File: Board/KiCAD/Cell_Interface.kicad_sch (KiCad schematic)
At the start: 26 parts, among them Q23 2N7002, Q24 2N7002, Q25 2N7002, Q26 2N7002, Q5 BSS83P, Q6 BSS83P, Q7 BSS83P, Q8 BSS83P, U6 INA219AxDCN, U7 INA219AxDCN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

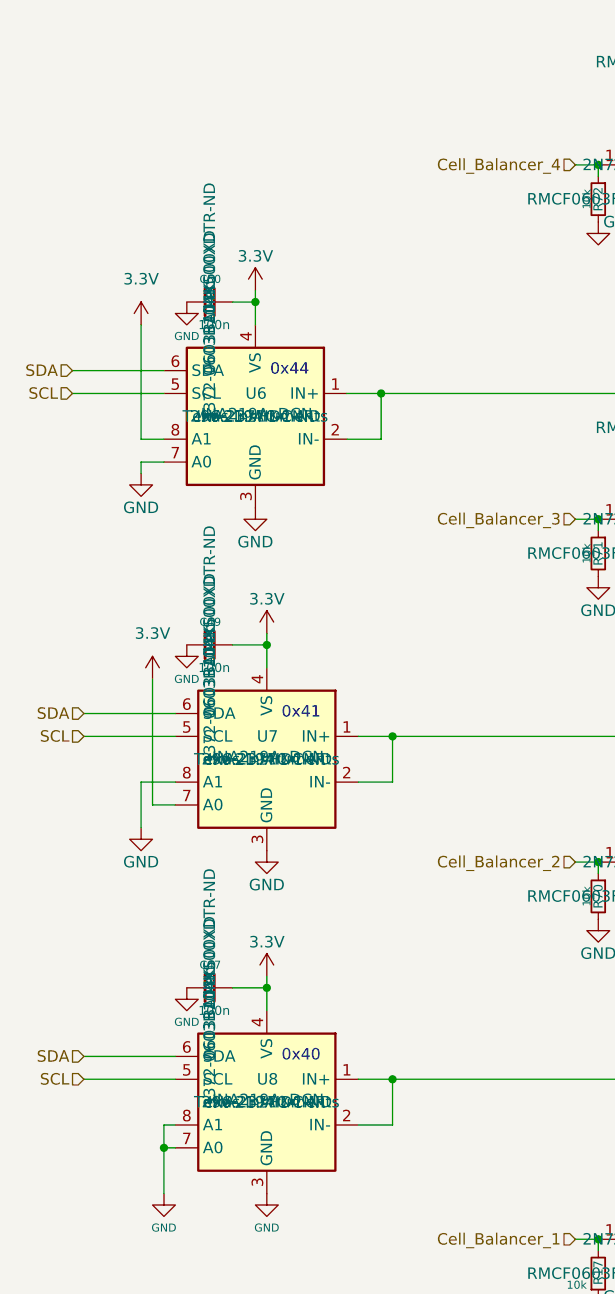
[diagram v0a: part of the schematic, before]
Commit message: Updated BOM as Per Ed's Request
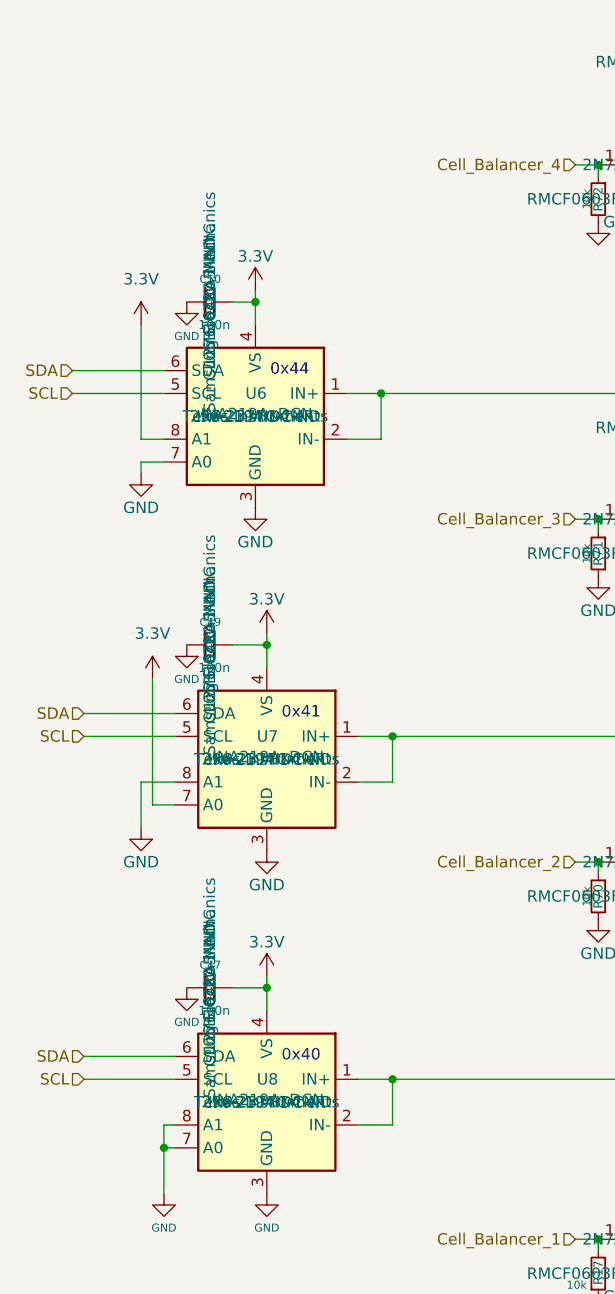
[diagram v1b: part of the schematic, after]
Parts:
- C47, C49, C50: MFR Aillen -> Samsung Electro-Mechanics; MPN 3372-0603B104K500XDTR-ND -> 1276-6720-1-ND; Package 0603B104K500XD -> CL05B104KA5NNNC
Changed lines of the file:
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@@
 			)
 		)
-		(property "Datasheet" "https://mm.digikey.com/Volume0/opasdata/d220001/medias/docus/6490/3372_0603B104K500XD.pdf"
+		(property "Datasheet" "https://mm.digikey.com/Volume0/opasdata/d220001/medias/docus/729/CL05B104KA5NNNC_Spec.pdf"
 			(at 63.5 137.16 0)
 			(effects
@@
 			)
 		)
-		(property "MFR" "Aillen"
+		(property "MFR" "Samsung Electro-Mechanics"
 			(at 63.5 137.16 0)
 			(effects
@@
 			)
 		)
-		(property "MPN" "3372-0603B104K500XDTR-ND"
+		(property "MPN" "1276-6720-1-ND"
 			(at 63.5 137.16 0)
 			(effects
@@
 			)
 		)
-		(property "Package" "0603B104K500XD"
+		(property "Package" "CL05B104KA5NNNC"
 			(at 63.5 137.16 0)
 			(effects
@@
 			)
 		)
-		(property "Datasheet" "https://mm.digikey.com/Volume0/opasdata/d220001/medias/docus/6490/3372_0603B104K500XD.pdf"
+		(property "Datasheet" "https://mm.digikey.com/Volume0/opasdata/d220001/medias/docus/729/CL05B104KA5NNNC_Spec.pdf"
 			(at 63.5 99.06 0)
 			(effects
@@
 			)
 		)
-		(property "MFR" "Aillen"
+		(property "MFR" "Samsung Electro-Mechanics"
 			(at 63.5 99.06 0)
 			(effects
@@
 			)
 		)
-		(property "MPN" "3372-0603B104K500XDTR-ND"
+		(property "MPN" "1276-6720-1-ND"
 			(at 63.5 99.06 0)
 			(effects
@@
 			)
 		)
-		(property "Package" "0603B104K500XD"
+		(property "Package" "CL05B104KA5NNNC"
 			(at 63.5 99.06 0)
 			(effects
@@
 			)
 		)
-		(property "Datasheet" "https://mm.digikey.com/Volume0/opasdata/d220001/medias/docus/6490/3372_0603B104K500XD.pdf"
+		(property "Datasheet" "https://mm.digikey.com/Volume0/opasdata/d220001/medias/docus/729/CL05B104KA5NNNC_Spec.pdf"
 			(at 63.5 60.96 0)
 			(effects
@@
 			)
 		)
-		(property "MFR" "Aillen"
+		(property "MFR" "Samsung Electro-Mechanics"
 			(at 63.5 60.96 0)
 			(effects
@@
 			)
 		)
-		(property "MPN" "3372-0603B104K500XDTR-ND"
+		(property "MPN" "1276-6720-1-ND"
 			(at 63.5 60.96 0)
 			(effects
@@
 			)
 		)
-		(property "Package" "0603B104K500XD"
+		(property "Package" "CL05B104KA5NNNC"
 			(at 63.5 60.96 0)
 			(effects

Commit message: non corrupt ver.
safsfs
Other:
- note added: "Edited"
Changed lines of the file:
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@@
+		)
+	)
+	(text "Edited"
+		(exclude_from_sim no)
+		(at 170.688 68.326 0)
+		(effects
+			(font
+				(size 1.27 1.27)
+			)
 		)
 	)

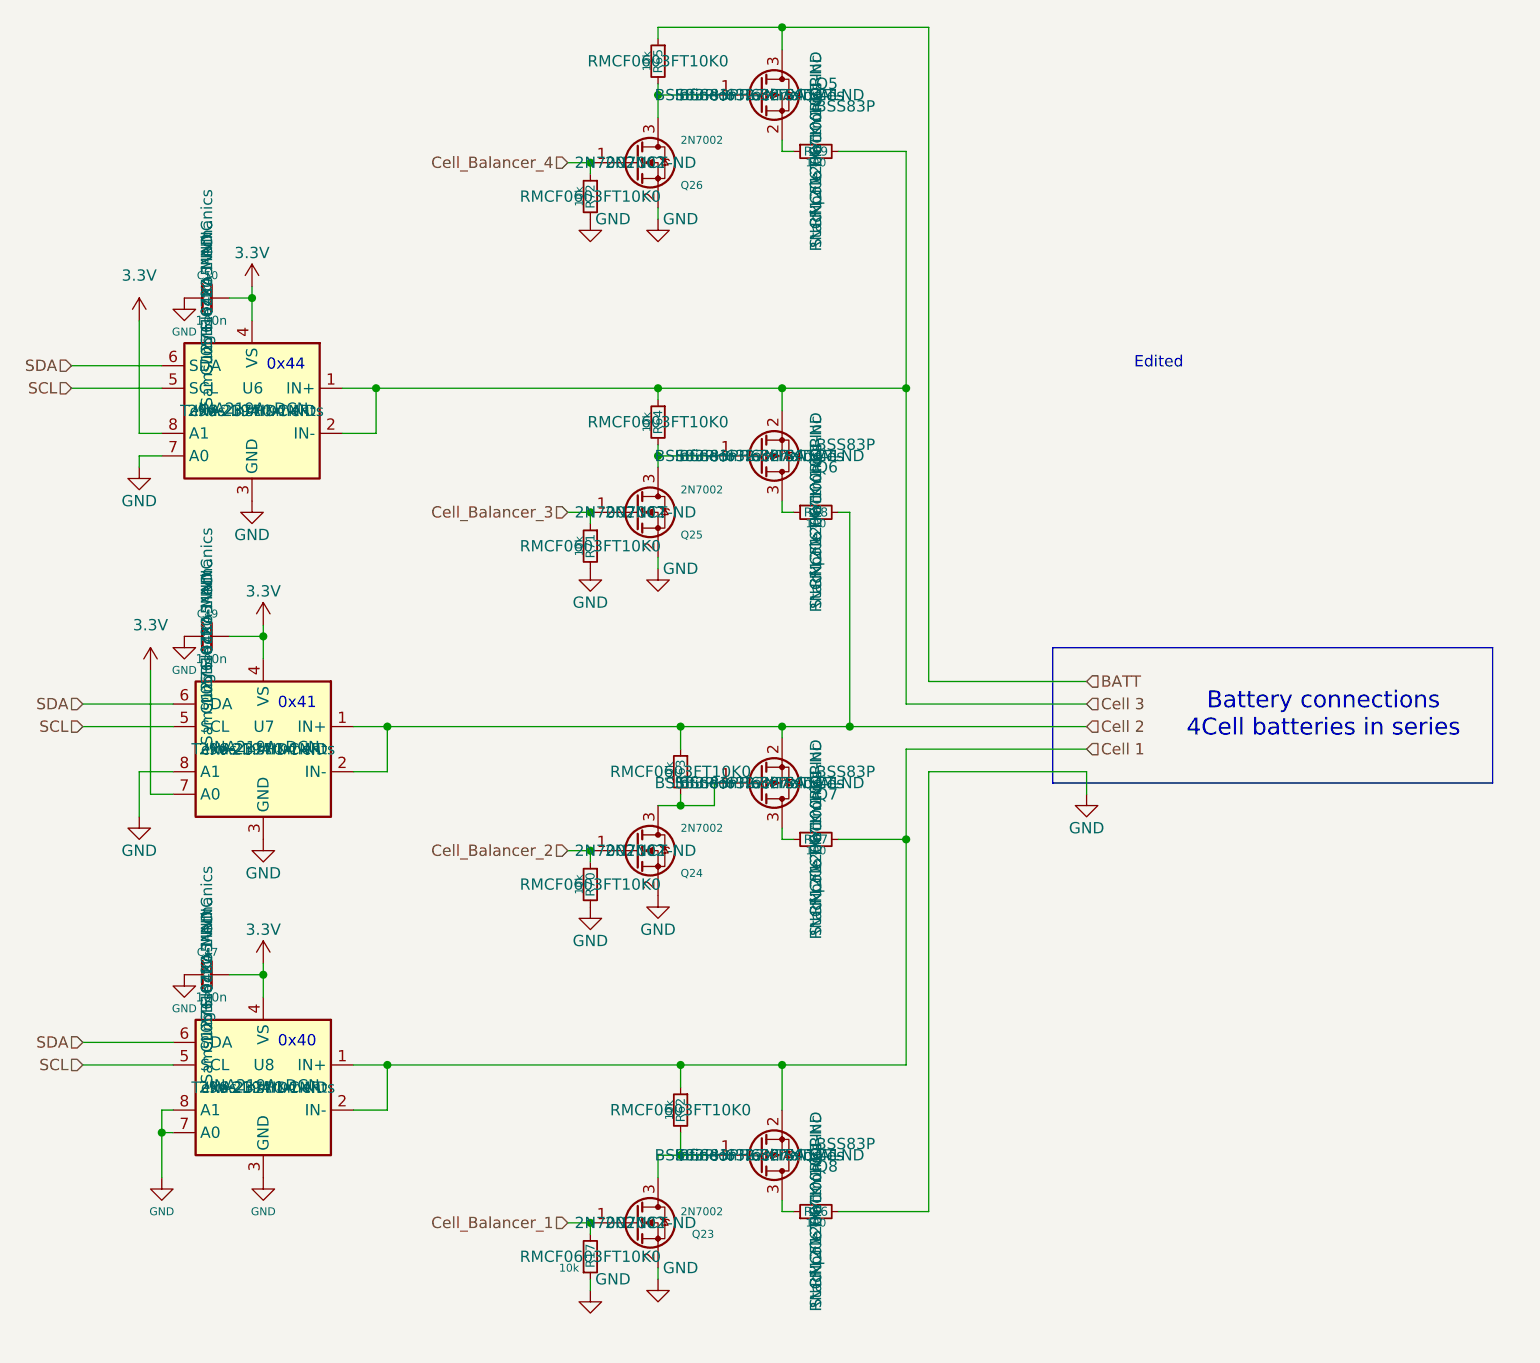
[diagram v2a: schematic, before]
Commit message: Cleaned up BOM materials again. Why do these keep reseting? Also, big refactor on cell balancing circuits and battery connection (NOW FLIPPED) to make board smaller. More smallification is left as an exercise to the reader.
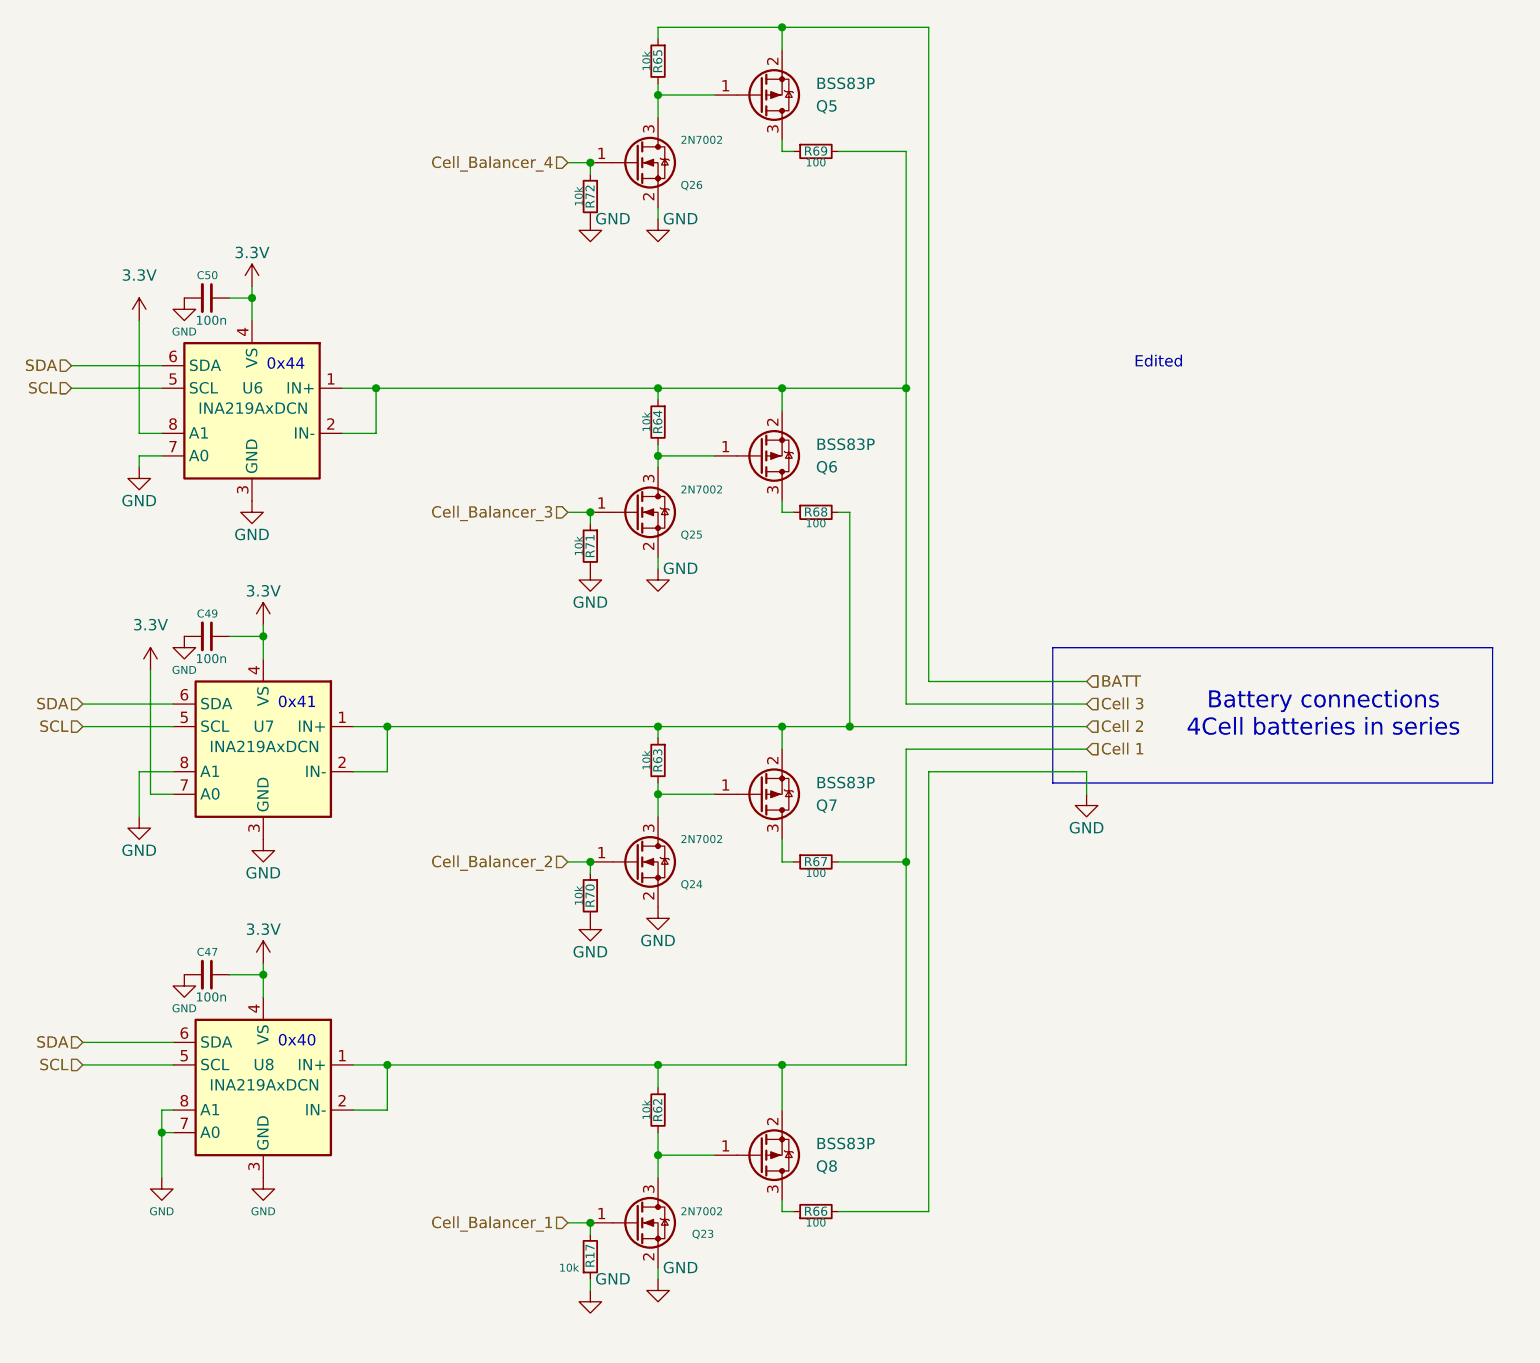
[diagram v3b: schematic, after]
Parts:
- C47, C49, C50: Package CL05B104KA5NNNC -> (none)
- Q23, Q24, Q25, Q26: Package 2N7002 -> (none)
- Q5, Q6, Q7, Q8: Package BSS83PH6327XTSA1 -> (none)
- R17, R62, R63, R64, R65, R70, R71, R72: Package RMCF0603FT10K0 -> (none)
- R66, R67, R68, R69: Package RNCF1206TKY100R -> (none)
- U6, U7, U8: Package INA219AIDCNR -> (none)
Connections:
- net BATT: now also Q5.2 (S); no longer Q5.3 (D)
- net at R69.1: now also Q5.3 (D); no longer Q5.2 (S)
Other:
- moved on the sheet: Q24, Q7, R62, R63, R67, R70
